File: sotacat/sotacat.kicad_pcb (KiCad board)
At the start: 2 copper layers, 20 x 37.5 mm, 17 parts, among them J1 54-00035, J2 JST-SH, SW1 SW_SPDT, U1 MOUDLE-SEEEDUINO-XIAO-ESP32C3

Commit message: v0.3 placement
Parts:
- removed R5: 10, Resistor_SMD:R_0603_1608Metric
- C1: value 10uF -> 22uF
- J2: footprint Connector_JST:JST_SH_SM02B-SRSS-TB_1x02-1MP_P1.00mm_Horizontal -> Connector_Molex:Molex_PicoBlade_53261-0271_1x02-1MP_P1.25mm_Horizontal
- moved D1 16.9 mm to (143.1, 86.7), turned to 0 degrees
- moved R6 15.1 mm to (143.1, 88.5), turned to 0 degrees
- moved D2 14.9 mm to (137.8, 101.2), turned to 0 degrees
- moved J2 12.7 mm to (128.7, 90.5), turned to -90 degrees
- moved R7 12.3 mm to (137.8, 99.2), turned to 0 degrees
- moved H1 10.2 mm to (151.1, 102.5)
- moved R3 10.1 mm to (137.7, 97.6), turned to 180 degrees
- moved R4 8.55 mm to (137.7, 95.8), turned to 0 degrees
- moved J1 7.37 mm to (142.2, 101.3)
- moved SW1 5.61 mm to (130.8, 99.6), turned to 0 degrees
- moved R1 4.43 mm to (134.2, 87.5)
- moved R2 4.43 mm to (135.9, 87.5)
- moved C2 4.43 mm to (137.7, 87.5)
- moved C1 2.86 mm to (133.9, 92.5), turned to -90 degrees
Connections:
- J2 pad MP: GND -> (no net)
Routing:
- net /VBAT_RAW: track 27.3 -> 0.00 mm, vias 2 -> 0
- net GND: track 11.2 -> 0.00 mm, vias 98 -> 39
- net /TXD: track 10.9 -> 0.00 mm
- net /RING1: track 10.0 -> 0.00 mm
- net VBAT: track 26.0 -> 18.7 mm, vias 2 -> 0
- net Net-(U1-PB09_A7_D7_RX): track 8.84 -> 1.75 mm
- net /TIP: track 6.38 -> 0.00 mm
- net Net-(U1-PA02_A0_D0): track 26.5 -> 22.5 mm
- net /LED_AMB_AN: track 22.6 -> 19.1 mm, vias 2 -> 1
- net Net-(D2-K): track 2.02 -> 0.00 mm
- net Net-(D1-K): track 1.77 -> 0.00 mm
- net 3V3: track 17.6 -> 16.4 mm, vias 2 -> 1
- net /nLED_BLU: track 14.6 -> 13.5 mm, vias 2 -> 1
- net /nLED_AMB_CAT: track 18.4 -> 17.4 mm, vias 2 -> 1
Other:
- outline, holes or cut-outs redrawn
- board text added: "CC-BY 4.0"
- board text added: "Concept by AB6D -- PCB by K5EM"
- board text added: "SOTACat PCB v0.3"
- board text removed: "+"
- board text removed: "G"
- board text removed: "SOTACat PCB v0.2 by K5EM"

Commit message: Just playing around with some v0.3 thoughts.
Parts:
- removed H1: M4 MountingHole, MountingHole:MountingHole_4.3mm_M4
- added REF**: Jack_3.5mm_CUI_SJ2-3593D-SMT_Horizontal, Connector_Audio:Jack_3.5mm_CUI_SJ2-3593D-SMT_Horizontal, F.Cu at (113.0, 82.0)
- J1: moved to B.Cu
- moved R6 19.6 mm to (127.5, 100.2), turned to 90 degrees
- moved D1 19.4 mm to (129.2, 100.2), turned to 90 degrees
- moved J2 11.8 mm to (140.5, 90.0), turned to 90 degrees
- moved SW1 6.84 mm to (128.2, 93.2), turned to -90 degrees
- moved C2 6.35 mm to (134.7, 93.0), turned to 180 degrees
- moved C1 5.63 mm to (133.0, 87.0), turned to 0 degrees
- moved R2 3.98 mm to (134.7, 91.2), turned to 180 degrees
- moved R3 2.21 mm to (137.0, 95.5), turned to 0 degrees
- moved R1 2.09 mm to (134.7, 89.5), turned to 0 degrees
- moved D2 1.96 mm to (135.9, 100.5), turned to -90 degrees
- moved R4 1.55 mm to (137.0, 97.2), turned to 180 degrees
- moved R7 1.32 mm to (137.5, 100.5), turned to -90 degrees
- moved J1 0.75 mm to (141.5, 101.4), turned to 180 degrees
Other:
- board size 20 x 37.5 mm -> 19.7 x 38.3 mm

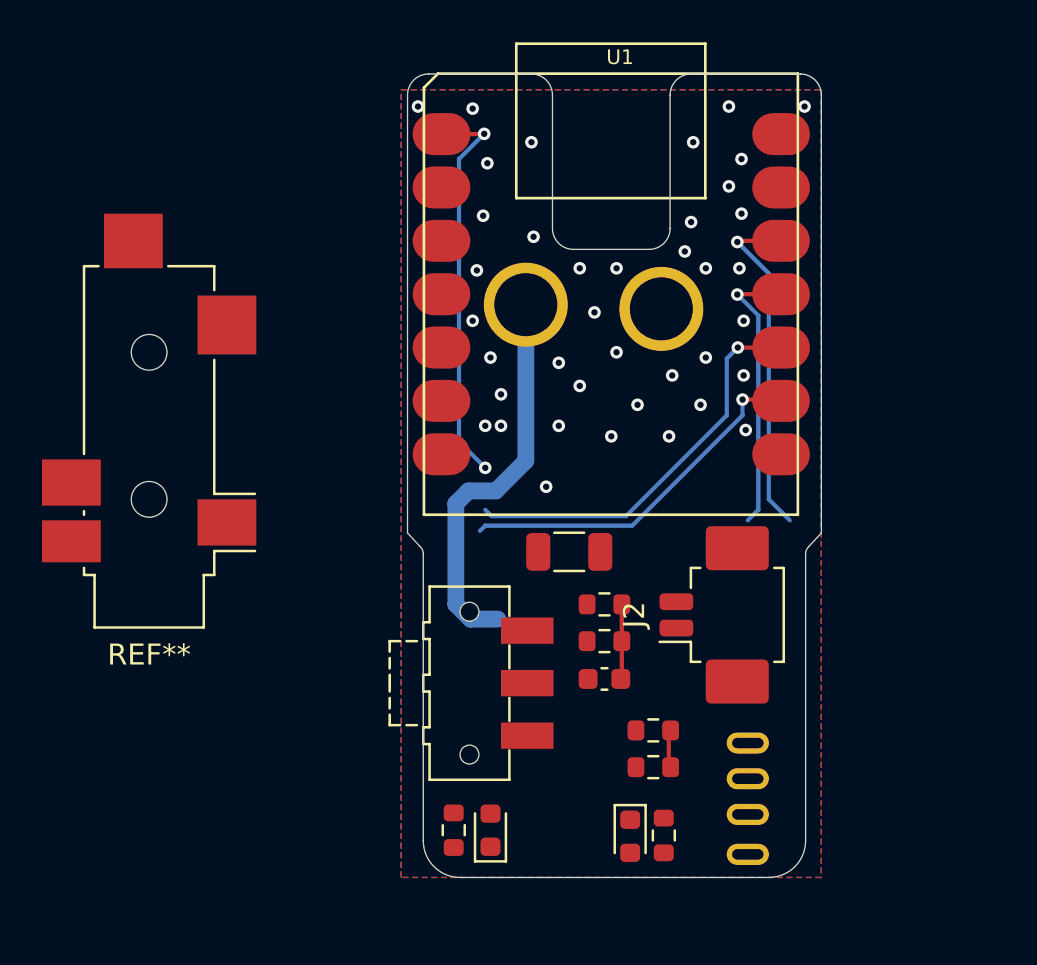
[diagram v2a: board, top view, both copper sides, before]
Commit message: Updates for Rev0.3. Breaking pin changes.
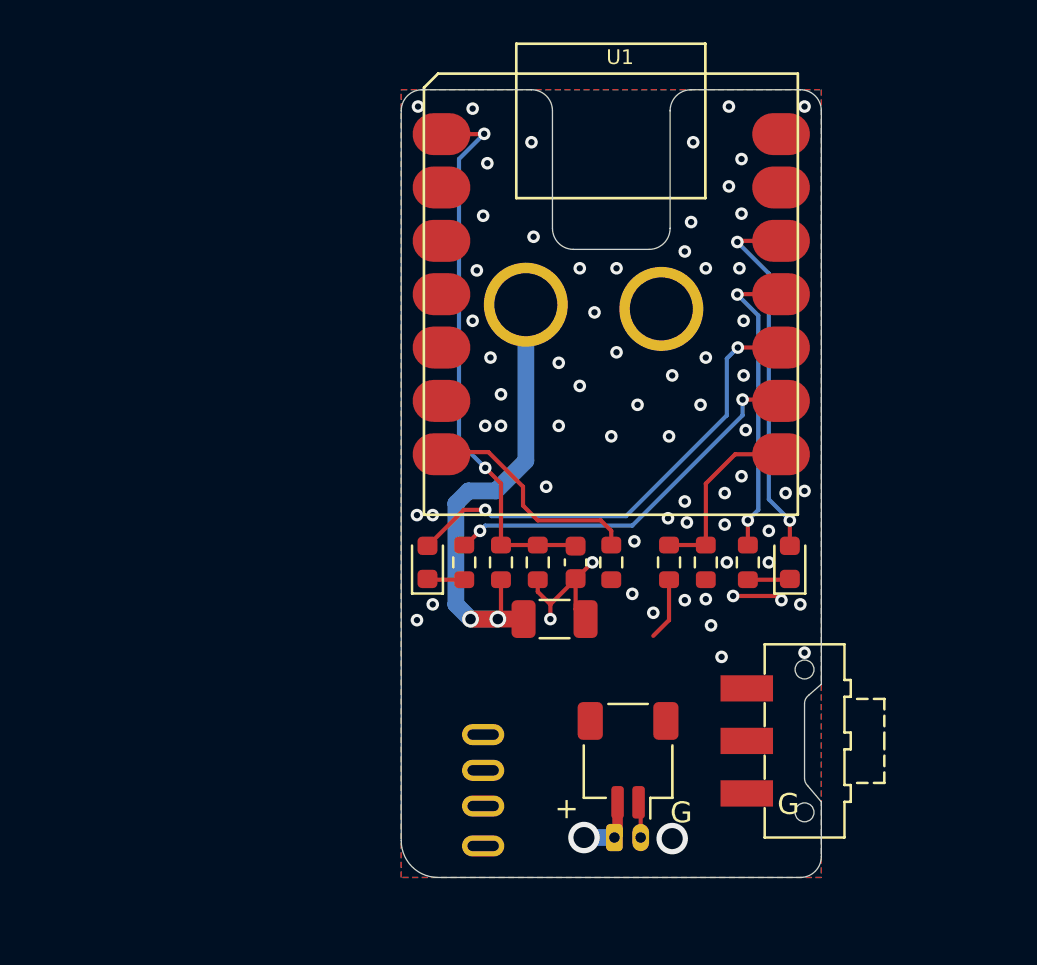
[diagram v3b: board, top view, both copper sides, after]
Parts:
- removed the REF** at (113.0, 82.0)
- added J3: PicoBlade, Connector_Molex:Molex_PicoBlade_53048-0210_1x02_P1.25mm_Horizontal, B.Cu at (135.2, 100.6)
- added R5: 10, Resistor_SMD:R_0603_1608Metric, F.Cu at (135.0, 87.5)
- J2: footprint Connector_Molex:Molex_PicoBlade_53261-0271_1x02-1MP_P1.25mm_Horizontal -> Connector_JST:JST_SH_SM02B-SRSS-TB_1x02-1MP_P1.00mm_Horizontal
- moved SW1 16.2 mm to (144.2, 96.0), turned to 90 degrees
- moved D2 15.1 mm to (143.5, 87.5), turned to 90 degrees
- moved R7 13.6 mm to (141.5, 87.5), turned to 90 degrees
- moved D1 13.1 mm to (126.2, 87.5)
- moved R6 12.8 mm to (128.0, 87.5)
- moved J1 12.6 mm to (128.9, 101.0)
- moved R4 10.1 mm to (139.5, 87.5), turned to -90 degrees
- moved J2 8.37 mm to (135.8, 96.9), turned to 180 degrees
- moved R3 8.04 mm to (137.8, 87.5), turned to 90 degrees
- moved C2 5.72 mm to (133.3, 87.5), turned to -90 degrees
- moved R1 5.32 mm to (129.8, 87.5), turned to 90 degrees
- moved R2 4.91 mm to (131.5, 87.5), turned to -90 degrees
- moved C1 3.28 mm to (132.3, 90.2)
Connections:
- J1 pad R2: unconnected-(J1-PadR2) -> GND
- J2 pad MP: (no net) -> GND
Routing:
- net GND: track 0.00 -> 11.2 mm, vias 39 -> 68
- net /TXD: track 0.00 -> 10.9 mm
- net Net-(U1-PB09_A7_D7_RX): track 1.75 -> 8.84 mm
- net VBAT: track 18.7 -> 23.1 mm, vias 0 -> 2
- net Net-(U1-PA02_A0_D0): track 22.5 -> 26.5 mm
- net /LED_AMB_AN: track 19.1 -> 22.6 mm, vias 1 -> 2
- net /VBAT_RAW: track 0.00 -> 3.23 mm, vias 0 -> 1
- net /RING1: track 0.00 -> 2.99 mm
- net Net-(D2-K): track 0.00 -> 2.02 mm
- net Net-(D1-K): track 0.00 -> 1.77 mm
- net 3V3: track 16.4 -> 17.6 mm, vias 1 -> 2
- net /nLED_BLU: track 13.5 -> 14.6 mm, vias 1 -> 2
- net /nLED_AMB_CAT: track 17.4 -> 18.4 mm, vias 1 -> 2
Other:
- board size 19.7 x 38.3 mm -> 20 x 37.5 mm
- board text added: "+"
- board text added: "Concept & SOTAMAT by AB6D"
- board text added: "G"
- board text added: "SOTACat PCB v0.3 by K5EM"
- board text removed: "CC-BY 4.0"
- board text removed: "Concept by AB6D -- PCB by K5EM"
- board text removed: "SOTACat PCB v0.3"

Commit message: PCB v0.3. Added MAX17260xxTD battery monitor, moved plug to corner, moved switch and LEDs accordingly. Changed pinout. Pinout not compatible with v0.2 due to TX data swap to avoid bootloader output.
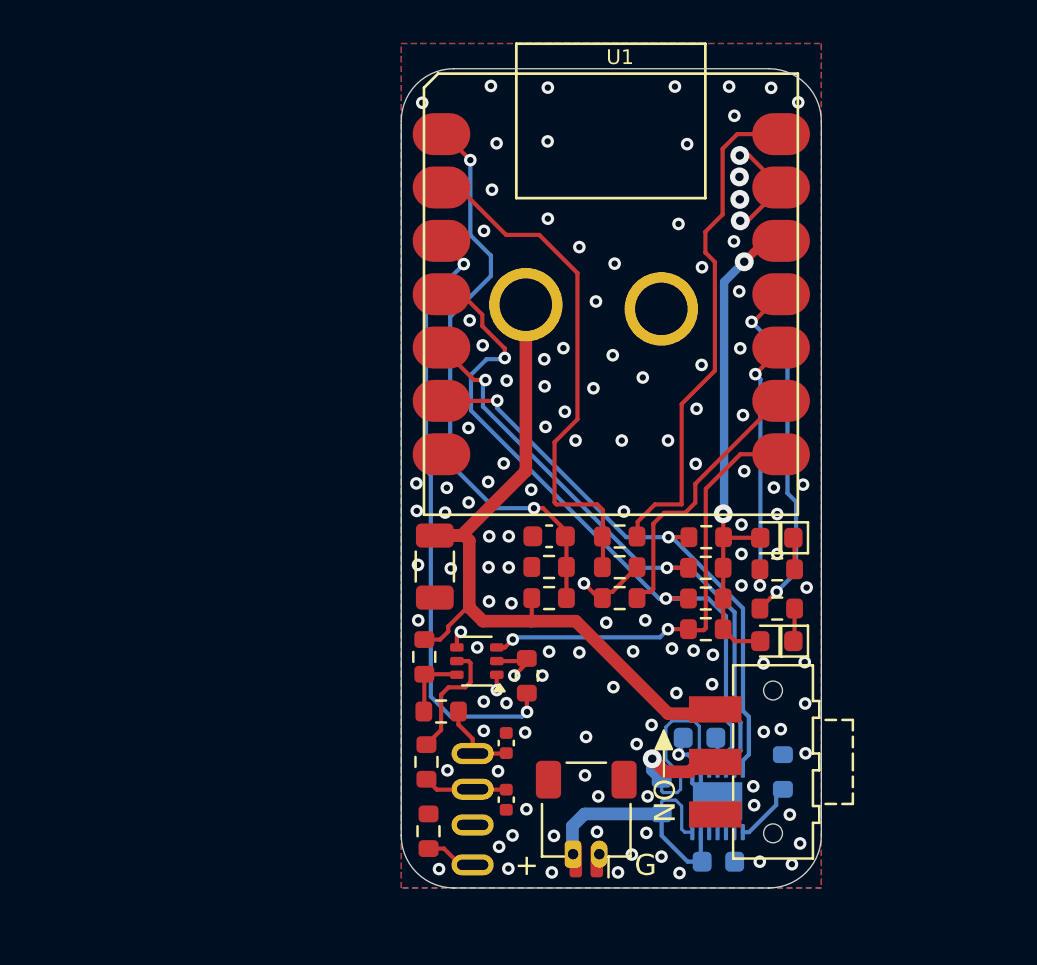
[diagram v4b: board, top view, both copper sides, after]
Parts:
- added C3: 0.1uF, Capacitor_SMD:C_0603_1608Metric, B.Cu at (140.1, 101.8)
- added C4: 0.47uF, Capacitor_SMD:C_0603_1608Metric, B.Cu at (139.2, 95.8)
- added C5: 30pF, Capacitor_SMD:C_0402_1005Metric, F.Cu at (130.0, 96.1)
- added C6: 30pF, Capacitor_SMD:C_0402_1005Metric, F.Cu at (130.0, 98.8)
- added Q1: MBT3904DW1, Package_TO_SOT_SMD:SOT-363_SC-70-6, F.Cu at (128.6, 92.2)
- added R10: 0, Resistor_SMD:R_0603_1608Metric, F.Cu at (126.3, 100.3)
- added R11: 10k, Resistor_SMD:R_0603_1608Metric, F.Cu at (126.1, 92.0)
- added R12: 10k, Resistor_SMD:R_0603_1608Metric, F.Cu at (126.2, 97.0)
- added R13: 4.7k, Resistor_SMD:R_0603_1608Metric, F.Cu at (139.5, 89.2)
- added R14: 4.7k, Resistor_SMD:R_0603_1608Metric, F.Cu at (139.5, 86.3)
- added R15: 4.7k, Resistor_SMD:R_0603_1608Metric, F.Cu at (139.5, 87.8)
- added R16: 10m, Resistor_SMD:R_0603_1608Metric, B.Cu at (137.4, 98.7)
- added R17: 130, Resistor_SMD:R_0603_1608Metric, F.Cu at (126.9, 94.6)
- added R8: 200k, Resistor_SMD:R_0603_1608Metric, F.Cu at (135.4, 87.7)
- added R9: 100k, Resistor_SMD:R_0603_1608Metric, F.Cu at (135.4, 86.3)
- added TH1: 10k NTC, Resistor_SMD:R_0603_1608Metric, B.Cu at (143.2, 97.5)
- added U3: MAX17260xxTD, Package_DFN_QFN:TDFN-14-1EP_3x3mm_P0.4mm_EP1.78x2.35mm, B.Cu at (140.1, 98.9)
- R3: value 5.1k -> 10k
- R4: value 3.6k -> 4.7k
- R5: value 10 -> 10k
- moved D1 16.7 mm to (142.9, 86.3), turned to 180 degrees
- moved R6 14.9 mm to (142.9, 87.8), turned to 180 degrees
- moved R5 6.73 mm to (131.0, 92.9), turned to -90 degrees
- moved C1 6.22 mm to (126.6, 87.7), turned to -90 degrees
- moved R4 4.44 mm to (135.4, 89.2), turned to 180 degrees
- moved REF** 3.90 mm to (135.2, 81.2)
- moved D2 3.80 mm to (142.9, 91.2), turned to 180 degrees
- moved R3 3.63 mm to (139.5, 90.7), turned to 0 degrees
- moved J2 3.43 mm to (133.8, 99.7)
- moved R1 2.85 mm to (132.0, 89.2), turned to 0 degrees
- moved R7 2.61 mm to (142.9, 89.7), turned to 180 degrees
- moved J3 2.12 mm to (133.2, 101.4)
- moved SW1 1.80 mm to (142.7, 97.0)
- moved C2 1.77 mm to (132.0, 86.3), turned to 180 degrees
- moved J1 1.03 mm to (128.4, 101.9)
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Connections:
- net Net-(U1-PA02_A0_D0) renamed /BAT_SENSE
- D1 pad 2: /LED_AMB_AN -> 3V3
- J1 pad R1: /RING1 -> /R1_KX_TX
- J1 pad S: GND -> Net-(J1-PadS)
- J1 pad T: /TIP -> /TIP_KX_RX
- R3 pad 1: /RING1 -> /K_TX_SC_RX
- R3 pad 2: Net-(U1-PB09_A7_D7_RX) -> 3V3
- R4 pad 1: Net-(U1-PB09_A7_D7_RX) -> /nDIS_BL_MSG
- R5 pad 1: /TIP -> Net-(Q1A-B1)
- R5 pad 2: /TXD -> /K_RX_SC_TX
- R6 pad 2: /nLED_AMB_CAT -> /nLED_AMB
- SW1 pad 1: VBAT -> unconnected-(SW1-A-Pad1)
- SW1 pad 2: /VBAT_RAW -> /VBAT_SENSE
- SW1 pad 3: unconnected-(SW1-C-Pad3) -> VBAT
- U1 pad 10: /LED_AMB_AN -> /nLED_AMB
- U1 pad 2: unconnected-(U1-PA4_A1_D1-Pad2) -> /USB_DETECT
- U1 pad 3: unconnected-(U1-PA10_A2_D2-Pad3) -> /K_RX_SC_TX
- U1 pad 4: unconnected-(U1-PA11_A3_D3-Pad4) -> /nALRT
- U1 pad 5: unconnected-(U1-PA8_A4_D4_SDA-Pad5) -> /I2C_SDA
- U1 pad 6: unconnected-(U1-PA9_A5_D5_SCL-Pad6) -> /I2C_SCL
- U1 pad 7: /TXD -> unconnected-(U1-PB08_A6_D6_TX-Pad7)
- U1 pad 8: Net-(U1-PB09_A7_D7_RX) -> /K_TX_SC_RX
- U1 pad 9: /nLED_AMB_CAT -> /nDIS_BL_MSG
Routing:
- net /nALRT: track 0.00 -> 33.3 mm, vias 0 -> 2
- net /K_RX_SC_TX: track 0.00 -> 28.9 mm, vias 0 -> 2
- net /I2C_SDA: track 0.00 -> 28.8 mm, vias 0 -> 2
- net /I2C_SCL: track 0.00 -> 27.6 mm, vias 0 -> 2
- net /USB_DETECT: track 0.00 -> 24.4 mm
- net 5V: track 0.00 -> 24.0 mm
- net /LED_AMB_AN: track 22.6 -> 0.00 mm, vias 2 -> 0
- net /K_TX_SC_RX: track 0.00 -> 21.3 mm, vias 0 -> 2
- net /nLED_AMB_CAT: track 18.4 -> 0.00 mm, vias 2 -> 0
- net /VBAT_SENSE: track 0.00 -> 13.6 mm, vias 0 -> 1
- net VBAT: track 23.1 -> 36.6 mm, vias 2 -> 0
- net /nDIS_BL_MSG: track 0.00 -> 13.0 mm
- net /nLED_AMB: track 0.00 -> 12.7 mm, vias 0 -> 2
- net /VBAT_RAW: track 3.23 -> 14.7 mm, vias 1 -> 0
- net /TXD: track 10.9 -> 0.00 mm
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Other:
- board size 20 x 37.5 mm -> 20 x 39 mm
